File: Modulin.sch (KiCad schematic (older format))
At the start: 25 parts

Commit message: Schematic for JUST making sound.
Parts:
- removed U?: MAX4587EUB+, symbol MAX4587EUB+
- added C?: 10u, symbol C
- added C? (x3): 0.1u, symbol C
- added C? (x2): 10n, symbol C
- added C? (x2): 1u, symbol C
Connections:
- net labels added: GNDA, GNDD
- net labels removed: GND
- wire segments 78 -> 159
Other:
- moved on the sheet: C?, J?, R?, SW?, U?

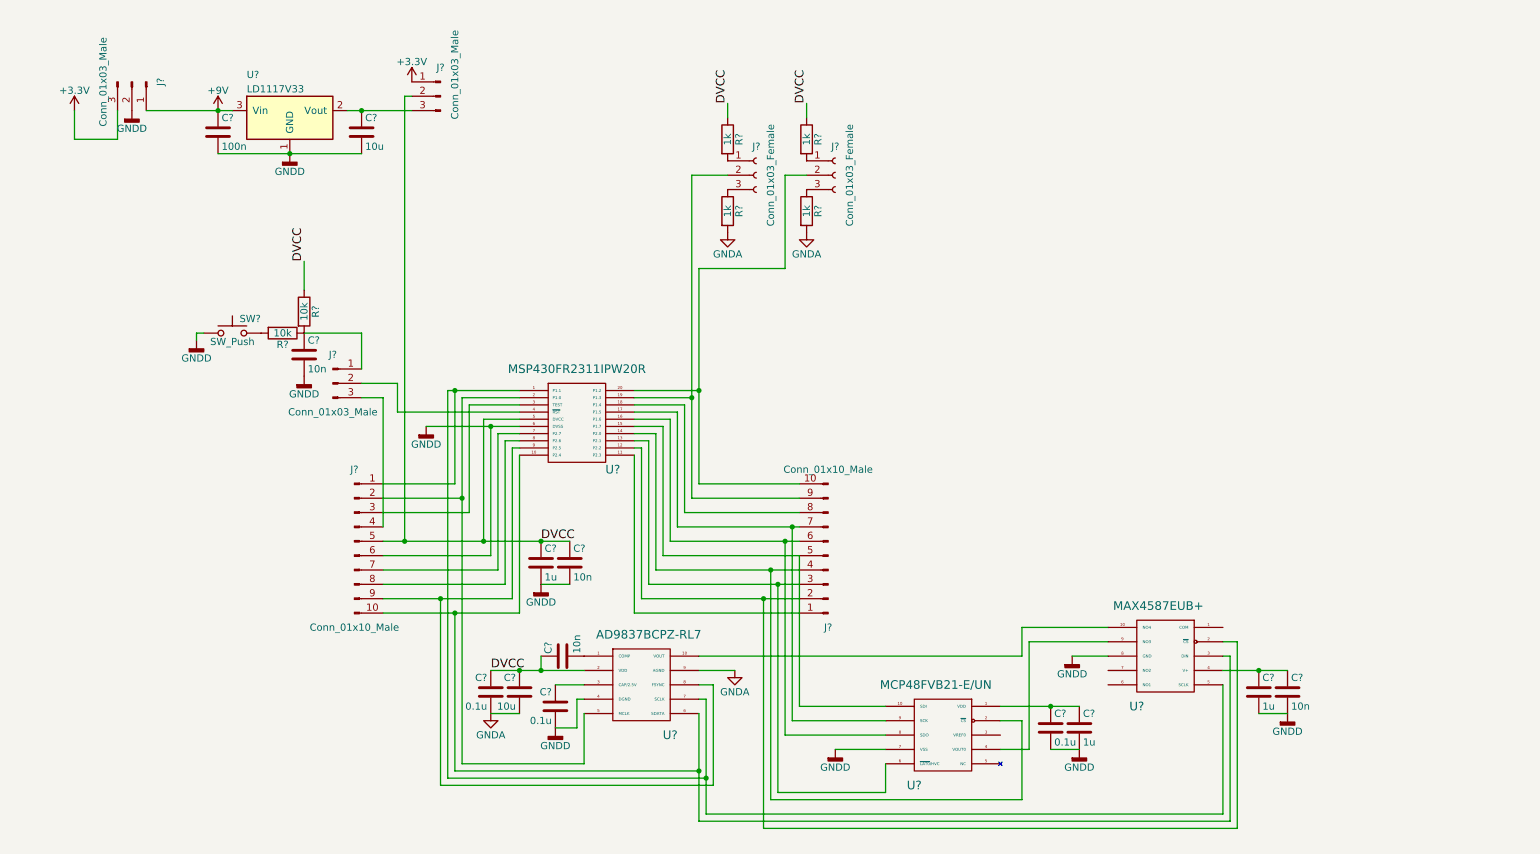
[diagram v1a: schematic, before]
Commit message: Moving towards distributed architecture and heirarchical schematic
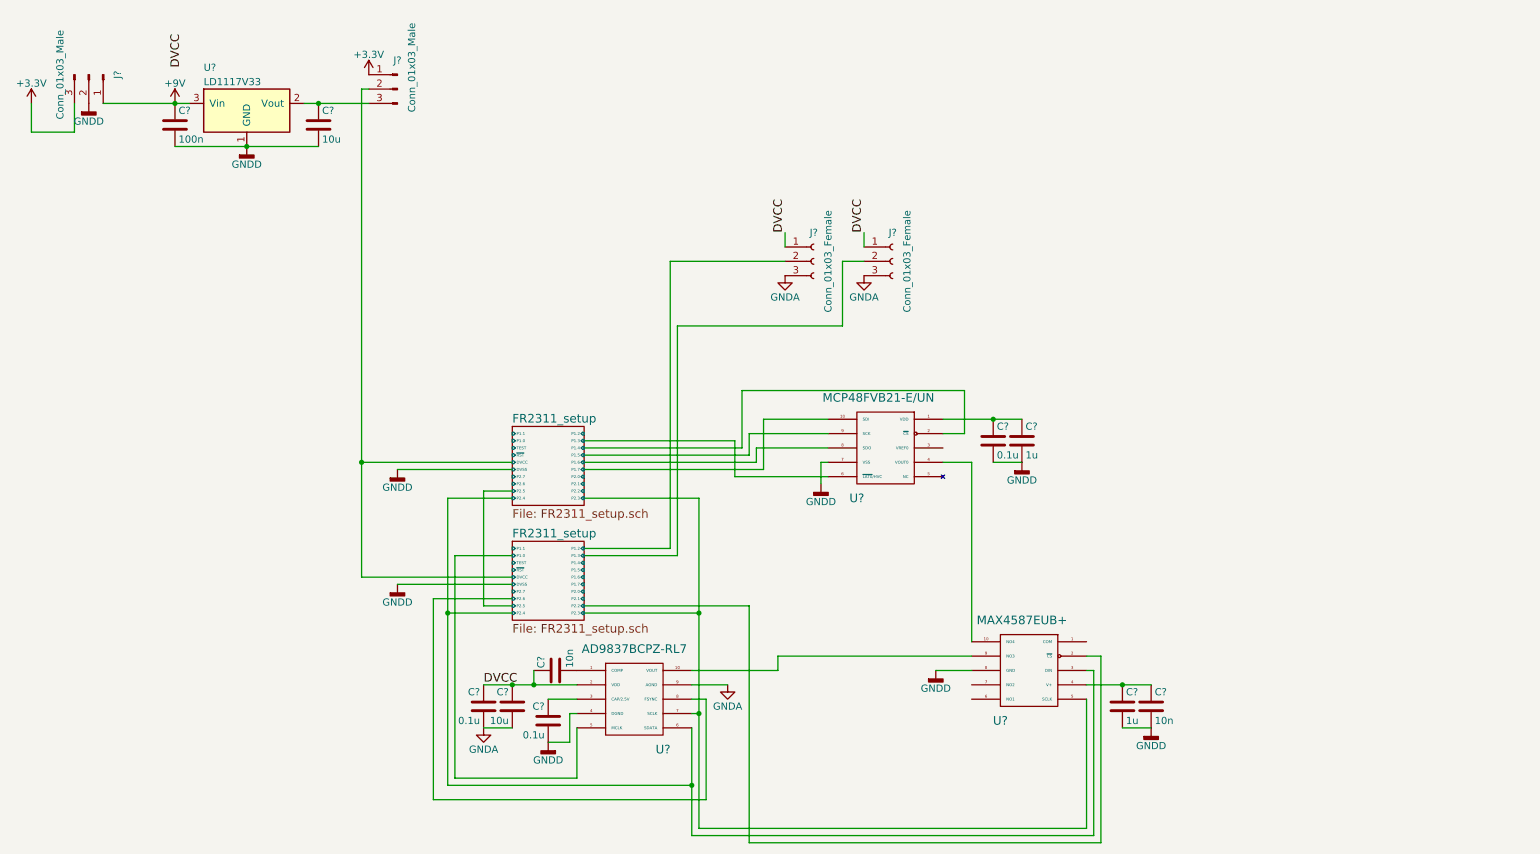
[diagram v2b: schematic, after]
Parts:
- removed C?: 1u, symbol C
- removed C? (x2): 10n, symbol C
- removed J? (x2): Conn_01x10_Male, symbol Conn_01x10_Male
- removed J?: Conn_01x03_Male, symbol Conn_01x03_Male
- removed J?: Conn_01x03_Female, symbol Conn_01x03_Female
- removed R? (x2): 10k, symbol R
- removed R? (x4): 1k, symbol R
- removed SW?: SW_Push, symbol SW_Push
- removed U?: MSP430FR2311IPW20R, symbol MSP430FR2311IPW20R
- added J?: Conn_01x03_Female, symbol Conn_01x03_Female
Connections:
- net DVCC: now also J?.1 (Pin_1), J?.1 (Pin_1); no longer J?.2 (Pin_2)
- net GNDA: now also J?.3 (Pin_3), J?.3 (Pin_3)
- net at U?.10 (NO4): now also U?.4 (VOUT0); no longer U?.10 (VOUT)
- net FR2311_setup/P2.2: now reaches U?.2 (~CS)
- net FR2311_setup/P2.4: now reaches U?.3 (DIN), U?.6 (SDATA)
- net FR2311_setup/P2.3: now reaches U?.5 (SCLK), U?.7 (SCLK)
- net at U?.9 (NO3): now also U?.10 (VOUT); no longer U?.4 (VOUT0)
- net FR2311_setup/P1.7: now reaches U?.10 (SDI)
- net FR2311_setup/P1.4: now reaches U?.2 (~CS)
- net FR2311_setup/P1.3: now reaches U?.6 (~LAT0~/HVC)
- net FR2311_setup/P1.6: now reaches U?.8 (SDO)
- net FR2311_setup/P1.5: now reaches U?.9 (SCK)
- net FR2311_setup/P1.0: now reaches U?.5 (MCLK)
- net FR2311_setup/P2.6: now reaches U?.8 (FSYNC)
- net FR2311_setup/P1.3: now reaches J?.2 (Pin_2)
- new net FR2311_setup/DVCC: J?.2 (Pin_2)
- new net FR2311_setup/P1.2: J?.2 (Pin_2)
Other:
- moved on the sheet: C?, J?, U?

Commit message: Added sheet for MIDI out
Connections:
- net FR2311_setup/P1.0 is gone; now on net FR2311_setup/P1.0: U?.5 (MCLK)
- net FR2311_setup/P1.2 is gone; now on net FR2311_setup/P1.2: J?.2 (Pin_2)
- net FR2311_setup/P1.3 is gone; now on net FR2311_setup/P1.3: J?.2 (Pin_2)
- net FR2311_setup/P1.4 is gone; now on net FR2311_setup/P1.4: U?.2 (~CS)
- net FR2311_setup/P1.5 is gone; now on net FR2311_setup/P1.5: U?.9 (SCK)
- net FR2311_setup/P1.6 is gone; now on net FR2311_setup/P1.6: U?.8 (SDO)
- net FR2311_setup/P1.7 is gone; now on net FR2311_setup/P1.7: U?.10 (SDI)
- net FR2311_setup/P2.2 is gone; now on net FR2311_setup/P2.2: U?.2 (~CS)
- net FR2311_setup/P2.6 is gone; now on net FR2311_setup/P2.6: U?.8 (FSYNC)
- net FR2311_setup/P1.3: no longer U?.6 (~LAT0~/HVC)
- new net FR2311_setup/P1.3: U?.6 (~LAT0~/HVC)
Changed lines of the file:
@@
 $Descr A4 11693 8268
 encoding utf-8
-Sheet 1 3
+Sheet 1 4
 Title "Modulin"
 Date "2017-11-19"
@@
 	4200 5250 4400 5250
 Wire Wire Line
-	5200 5450 5200 5850
-Wire Wire Line
-	5200 5850 5200 6200
+	5200 5450 5200 6200
 Wire Wire Line
 	3950 5450 3750 5450
 Connection ~ 3950 5150
 Wire Wire Line
-	3750 5150 3950 5150
-Wire Wire Line
-	3950 5150 4100 5150
-Wire Wire Line
-	4100 5150 4400 5150
+	3750 5150 4400 5150
 Wire Wire Line
 	5200 5150 5450 5150
@@
 Connection ~ 2100 1400
 Wire Wire Line
-	1600 1400 2100 1400
-Wire Wire Line
-	2100 1400 2600 1400
-Wire Wire Line
-	2500 1100 2600 1100
-Wire Wire Line
-	2600 1100 2950 1100
-Wire Wire Line
-	1100 1100 1600 1100
-Wire Wire Line
-	1600 1100 1700 1100
+	1600 1400 2600 1400
+Wire Wire Line
+	2500 1100 2950 1100
+Wire Wire Line
+	1100 1100 1700 1100
 Wire Wire Line
 	4400 5450 4400 5800
@@
 	5250 5350 5200 5350
 Wire Wire Line
-	5250 3850 5250 4650
-Wire Wire Line
-	5250 4650 5250 5350
-Wire Wire Line
-	5250 5350 5250 6150
+	5250 3850 5250 6150
 Wire Wire Line
 	6400 2200 6250 2200
@@
 	7300 3600 7500 3600
 Wire Wire Line
-	6950 3300 7300 3300
-Wire Wire Line
-	7300 3300 7500 3300
+	6950 3300 7500 3300
 Connection ~ 7300 3300
 Wire Wire Line
 	8200 5450 8400 5450
 Wire Wire Line
-	7950 5150 8200 5150
-Wire Wire Line
-	8200 5150 8400 5150
+	7950 5150 8400 5150
 Connection ~ 8200 5150
 Wire Wire Line
@@
 	3550 4250 3950 4250
 Wire Wire Line
-	3500 3850 3500 4650
-Wire Wire Line
-	3500 4650 3500 5850
+	3500 3850 3500 5850
 Wire Wire Line
 	3500 4650 3950 4650
@@
 	3750 3800 3950 3800
 Wire Wire Line
-	2900 1000 2900 3600
-Wire Wire Line
-	2900 3600 2900 4400
+	2900 1000 2900 4400
 Wire Wire Line
 	2900 3600 3950 3600
@@
 Wire Wire Line
 	6250 2650 6250 2200
+$Sheet
+S 5950 4250 500  300
+U 5A18B549
+F0 "MIDI_out" 60
+F1 "MIDI_out.sch" 60
+$EndSheet
 $EndSCHEMATC

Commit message: update to MIDI out sheet
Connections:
- net FR2311_setup/P1.0 is gone; now on net FR2311_setup/P1.0: U?.5 (MCLK)
- net FR2311_setup/P1.2 is gone; now on net FR2311_setup/P1.2: J?.2 (Pin_2)
- net FR2311_setup/P1.3 is gone; now on net FR2311_setup/P1.3: J?.2 (Pin_2)
- net FR2311_setup/P1.4 is gone; now on net FR2311_setup/P1.4: U?.2 (~CS)
- net FR2311_setup/P1.5 is gone; now on net FR2311_setup/P1.5: U?.9 (SCK)
- net FR2311_setup/P1.6 is gone; now on net FR2311_setup/P1.6: U?.8 (SDO)
- net FR2311_setup/P1.7 is gone; now on net FR2311_setup/P1.7: U?.10 (SDI)
- net FR2311_setup/P2.2 is gone; now on net FR2311_setup/P2.2: U?.2 (~CS)
- net FR2311_setup/P2.6 is gone; now on net FR2311_setup/P2.6: U?.8 (FSYNC)
- net FR2311_setup/P1.3: no longer U?.6 (~LAT0~/HVC)
- new net FR2311_setup/P1.3: U?.6 (~LAT0~/HVC)
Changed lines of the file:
@@
 LIBS:cmos4000
 LIBS:conn
-LIBS:logo
 LIBS:microchip_dspic33dsc
 LIBS:microchip_pic10mcu
@@
 LIBS:microchip_pic32mcu
 LIBS:msp430
-LIBS:MyLib
 LIBS:nxp_armmcu
 LIBS:relays
@@
 LIBS:ttl_ieee
 LIBS:valves
-LIBS:ac-dc
-LIBS:adc-dac
-LIBS:Altera
-LIBS:analog_devices
-LIBS:analog_switches
-LIBS:atmel
-LIBS:audio
-LIBS:Battery_Management
-LIBS:bbd
-LIBS:bosch
-LIBS:brooktre
-LIBS:Connector
-LIBS:contrib
-LIBS:cypress
-LIBS:dc-dc
-LIBS:device
-LIBS:digital-audio
-LIBS:Diode
-LIBS:Display
-LIBS:driver_gate
-LIBS:dsp
-LIBS:DSP_Microchip_DSPIC33
-LIBS:elec-unifil
-LIBS:ESD_Protection
-LIBS:Espressif
-LIBS:FPGA_Actel
-LIBS:ftdi
-LIBS:gennum
-LIBS:Graphic
-LIBS:hc11
-LIBS:infineon
-LIBS:intel
-LIBS:interface
-LIBS:intersil
-LIBS:ir
-LIBS:Lattice
-LIBS:LED
-LIBS:LEM
-LIBS:linear
-LIBS:Logic_74xgxx
-LIBS:Logic_74xx
-LIBS:Logic_CMOS_4000
-LIBS:Logic_CMOS_IEEE
-LIBS:logic_programmable
-LIBS:Logic_TTL_IEEE
-LIBS:maxim
-LIBS:MCU_Microchip_PIC10
-LIBS:MCU_Microchip_PIC12
-LIBS:MCU_Microchip_PIC16
-LIBS:MCU_Microchip_PIC18
-LIBS:MCU_Microchip_PIC24
-LIBS:MCU_Microchip_PIC32
-LIBS:MCU_NXP_Kinetis
-LIBS:MCU_NXP_LPC
-LIBS:MCU_NXP_S08
-LIBS:MCU_ST_STM8
-LIBS:MCU_ST_STM32
-LIBS:MCU_Texas_MSP430
-LIBS:Mechanical
-LIBS:memory
-LIBS:microchip
-LIBS:microcontrollers
-LIBS:modules
-LIBS:Motor
-LIBS:motor_drivers
-LIBS:motorola
-LIBS:nordicsemi
-LIBS:nxp
-LIBS:onsemi
-LIBS:opto
-LIBS:Oscillators
-LIBS:philips
-LIBS:power
-LIBS:Power_Management
-LIBS:powerint
-LIBS:pspice
-LIBS:references
-LIBS:regul
-LIBS:Relay
-LIBS:rfcom
-LIBS:RFSolutions
-LIBS:Sensor_Current
-LIBS:sensors
-LIBS:silabs
-LIBS:siliconi
-LIBS:supertex
-LIBS:Switch
-LIBS:texas
-LIBS:Transformer
-LIBS:Transistor
-LIBS:triac_thyristor
-LIBS:Valve
-LIBS:video
-LIBS:wiznet
-LIBS:Worldsemi
-LIBS:Xicor
-LIBS:xilinx
-LIBS:zetex
-LIBS:Zilog
 LIBS:Modulin-cache
 EELAYER 25 0

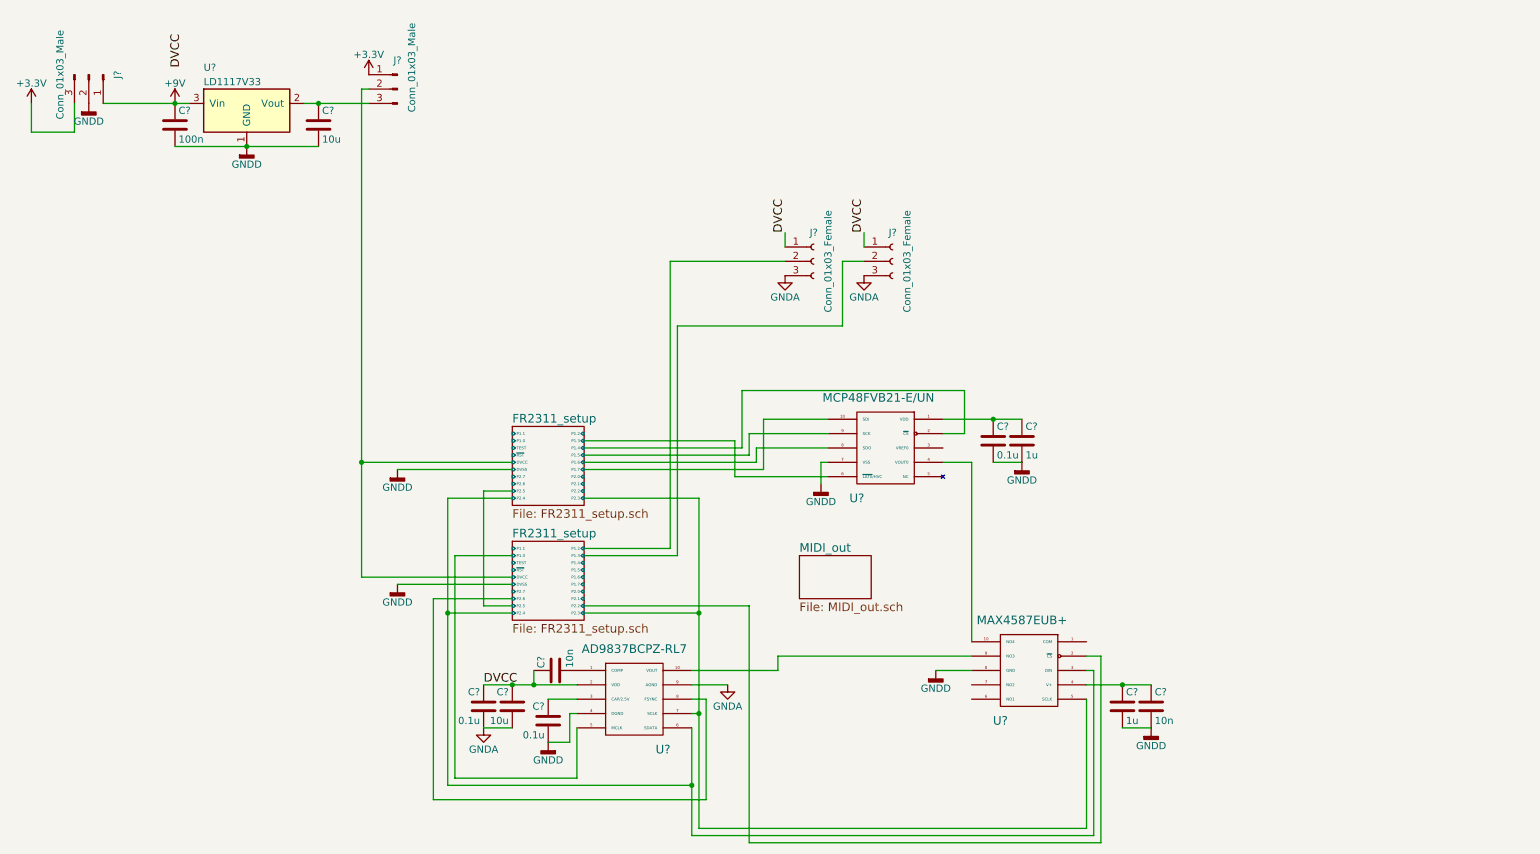
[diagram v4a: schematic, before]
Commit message: Added circuit for encoder
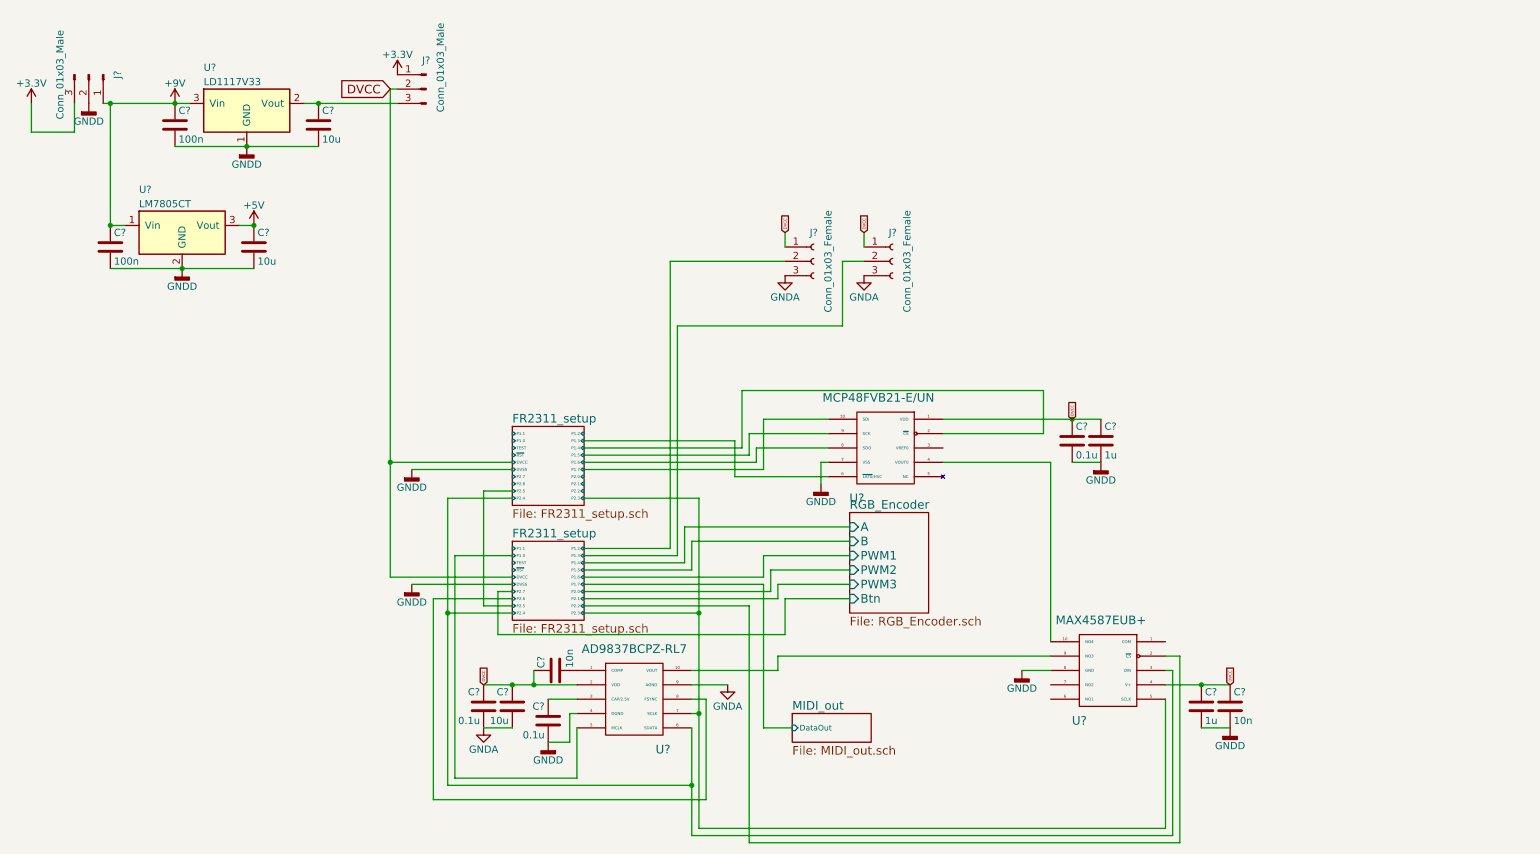
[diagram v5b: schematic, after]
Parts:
- added C?: 100n, symbol C
- added C?: 10u, symbol C
- added U?: LM7805CT, TO-220-3, symbol LM7805CT
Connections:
- net FR2311_setup/DVCC is gone; now on net DVCC: J?.2 (Pin_2)
- net FR2311_setup/P1.0 is gone; now on net FR2311_setup/P1.0: U?.5 (MCLK)
- net FR2311_setup/P1.2 is gone; now on net FR2311_setup/P1.2: J?.2 (Pin_2)
- net FR2311_setup/P1.3 is gone; now on net FR2311_setup/P1.3: J?.2 (Pin_2)
- net FR2311_setup/P1.4 is gone; now on net FR2311_setup/P1.4: U?.2 (~CS)
- net FR2311_setup/P1.5 is gone; now on net FR2311_setup/P1.5: U?.9 (SCK)
- net FR2311_setup/P1.6 is gone; now on net FR2311_setup/P1.6: U?.8 (SDO)
- net FR2311_setup/P1.7 is gone; now on net FR2311_setup/P1.7: U?.10 (SDI)
- net FR2311_setup/P2.2 is gone; now on net FR2311_setup/P2.2: U?.2 (~CS)
- net FR2311_setup/P2.6 is gone; now on net FR2311_setup/P2.6: U?.8 (FSYNC)
- net +9V: now also C?.1, U?.1 (Vin)
- net DVCC: now also C?.1, C?.1, C?.1, C?.1, U?.1 (VDD), U?.4 (V+)
- net FR2311_setup/P1.3: no longer U?.6 (~LAT0~/HVC)
- net GNDD: now also C?.2, C?.2, U?.2 (GND)
- new net +5V: C?.1, U?.3 (Vout)
- new net FR2311_setup/P1.3: U?.6 (~LAT0~/HVC)
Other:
- moved on the sheet: C?, J?, U?
